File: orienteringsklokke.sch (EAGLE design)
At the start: 15 parts

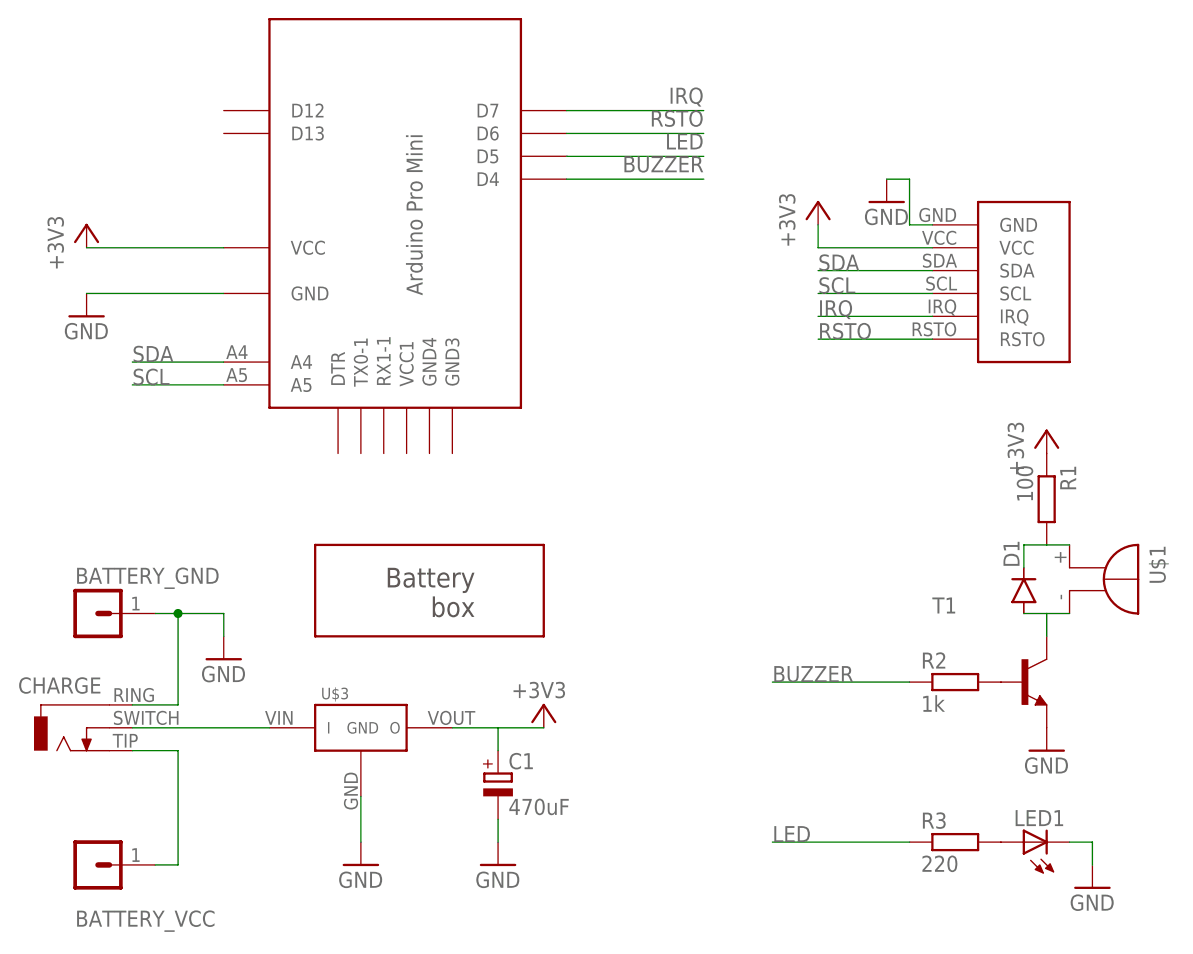
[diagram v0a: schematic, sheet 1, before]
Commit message: Fully traced with jack, switch, buzzer and no battery box
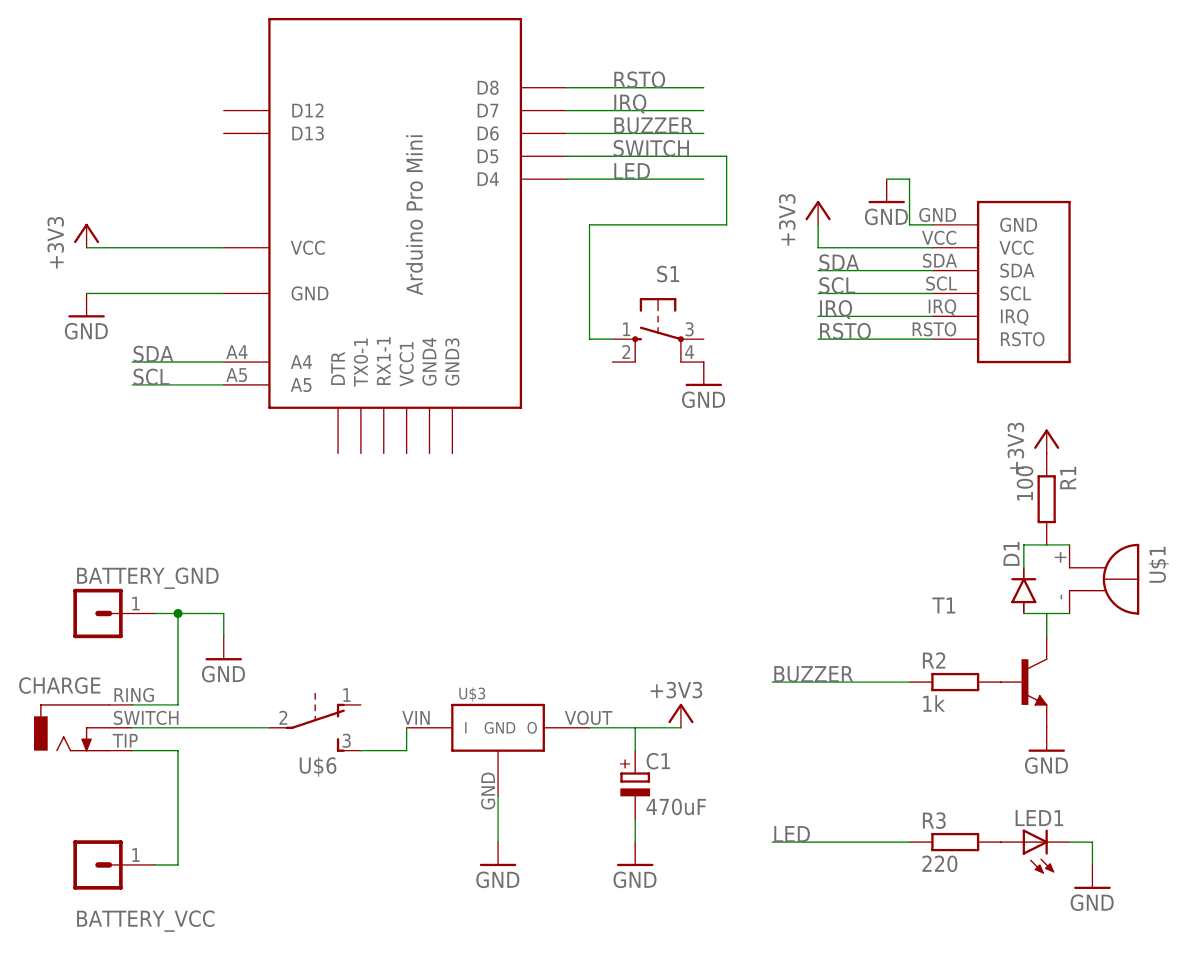
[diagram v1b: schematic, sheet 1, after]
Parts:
- removed U$5: BATTERY-BOX, joakim:BATTERY-BOX
- added S1: (no value), switch-omron:10-XX
- added U$6: SK12D07-SLIDE-SWITCH, joakim:SK12D07-SLIDE-SWITCH
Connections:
- new net N$1: CHARGE.2, U$6.2
- new net SWITCH: S1.S, U$4.D5
- net BUZZER: now also U$4.D6; no longer U$4.D4
- net GND: now also S1.P1
- net LED: now also U$4.D4; no longer U$4.D5
- net N$7: now also U$6.3; no longer CHARGE.2
- net RSTO: now also U$4.D8; no longer U$4.D6
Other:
- moved on the sheet: C1, U$3
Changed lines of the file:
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@@
 <part name="GND7" library="supply1" deviceset="GND" device=""/>
 <part name="CHARGE" library="joakim" deviceset="ST613-JACK" device=""/>
-<part name="U$5" library="joakim" deviceset="BATTERY-BOX" device=""/>
+<part name="S1" library="switch-omron" deviceset="10-XX" device=""/>
+<part name="GND8" library="supply1" deviceset="GND" device=""/>
+<part name="U$6" library="joakim" deviceset="SK12D07-SLIDE-SWITCH" device=""/>
 </parts>
 <sheets>
@@
 </instance>
 <instance part="R3" gate="G$1" x="60.96" y="25.4"/>
-<instance part="C1" gate="G$1" x="10.16" y="33.02"/>
+<instance part="C1" gate="G$1" x="25.4" y="33.02"/>
 <instance part="GND1" gate="1" x="71.12" y="35.56"/>
 <instance part="D1" gate="G$1" x="68.58" y="53.34" smashed="yes" rot="R90">
@@
 <instance part="LED1" gate="G$1" x="68.58" y="25.4" rot="R90"/>
 <instance part="GND2" gate="1" x="76.2" y="20.32"/>
-<instance part="U$3" gate="G$1" x="-5.08" y="38.1"/>
-<instance part="GND3" gate="1" x="-5.08" y="22.86"/>
-<instance part="GND4" gate="1" x="10.16" y="22.86"/>
-<instance part="+3V2" gate="G$1" x="15.24" y="40.64" smashed="yes">
-<attribute name="VALUE" x="17.78" y="43.18" size="1.778" layer="96" rot="R180"/>
+<instance part="U$3" gate="G$1" x="10.16" y="38.1"/>
+<instance part="GND3" gate="1" x="10.16" y="22.86"/>
+<instance part="GND4" gate="1" x="25.4" y="22.86"/>
+<instance part="+3V2" gate="G$1" x="30.48" y="40.64" smashed="yes">
+<attribute name="VALUE" x="33.02" y="43.18" size="1.778" layer="96" rot="R180"/>
 </instance>
 <instance part="GND5" gate="1" x="-20.32" y="45.72"/>
@@
 <attribute name="NAME" x="-43.18" y="41.91" size="1.778" layer="95"/>
 </instance>
-<instance part="U$5" gate="G$1" x="2.54" y="53.34" rot="R180"/>
+<instance part="S1" gate="1" x="27.94" y="81.28" rot="MR270"/>
+<instance part="GND8" gate="1" x="33.02" y="76.2"/>
+<instance part="U$6" gate="G$1" x="-10.16" y="38.1"/>
 </instances>
 <busses>
@@
 <pinref part="U$3" gate="G$1" pin="GND"/>
 <pinref part="GND3" gate="1" pin="GND"/>
-<wire x1="-5.08" y1="25.4" x2="-5.08" y2="30.48" width="0.1524" layer="91"/>
+<wire x1="10.16" y1="25.4" x2="10.16" y2="30.48" width="0.1524" layer="91"/>
 </segment>
 <segment>
 <pinref part="C1" gate="G$1" pin="-"/>
 <pinref part="GND4" gate="1" pin="GND"/>
-<wire x1="10.16" y1="27.94" x2="10.16" y2="25.4" width="0.1524" layer="91"/>
+<wire x1="25.4" y1="27.94" x2="25.4" y2="25.4" width="0.1524" layer="91"/>
 </segment>
 <segment>
@@
 <pinref part="GND7" gate="1" pin="GND"/>
 </segment>
+<segment>
+<pinref part="S1" gate="1" pin="P1"/>
+<pinref part="GND8" gate="1" pin="GND"/>
+</segment>
 </net>
 <net name="N$2" class="0">
@@
 <pinref part="U$3" gate="G$1" pin="VOUT"/>
 <pinref part="C1" gate="G$1" pin="+"/>
-<wire x1="5.08" y1="38.1" x2="10.16" y2="38.1" width="0.1524" layer="91"/>
-<wire x1="10.16" y1="35.56" x2="10.16" y2="38.1" width="0.1524" layer="91"/>
-<wire x1="10.16" y1="38.1" x2="15.24" y2="38.1" width="0.1524" layer="91"/>
+<wire x1="20.32" y1="38.1" x2="25.4" y2="38.1" width="0.1524" layer="91"/>
+<wire x1="25.4" y1="35.56" x2="25.4" y2="38.1" width="0.1524" layer="91"/>
+<wire x1="25.4" y1="38.1" x2="30.48" y2="38.1" width="0.1524" layer="91"/>
 <pinref part="+3V2" gate="G$1" pin="+3V3"/>
 </segment>
@@
 </segment>
 <segment>
-<pinref part="U$4" gate="G$1" pin="D4"/>
-<wire x1="17.78" y1="99.06" x2="33.02" y2="99.06" width="0.1524" layer="91"/>
-<label x="33.02" y="101.6" size="1.778" layer="95" rot="R180"/>
+<pinref part="U$4" gate="G$1" pin="D6"/>
+<wire x1="17.78" y1="104.14" x2="33.02" y2="104.14" width="0.1524" layer="91"/>
+<label x="22.86" y="104.14" size="1.778" layer="95"/>
 </segment>
 </net>
@@
 </segment>
 <segment>
-<pinref part="U$4" gate="G$1" pin="D5"/>
-<wire x1="17.78" y1="101.6" x2="33.02" y2="101.6" width="0.1524" layer="91"/>
-<label x="33.02" y="104.14" size="1.778" layer="95" rot="R180"/>
+<pinref part="U$4" gate="G$1" pin="D4"/>
+<wire x1="17.78" y1="99.06" x2="33.02" y2="99.06" width="0.1524" layer="91"/>
+<label x="22.86" y="99.06" size="1.778" layer="95"/>
 </segment>
 </net>
@@
 <pinref part="U$4" gate="G$1" pin="D7"/>
 <wire x1="17.78" y1="106.68" x2="33.02" y2="106.68" width="0.1524" layer="91"/>
-<label x="33.02" y="109.22" size="1.778" layer="95" rot="R180"/>
+<label x="22.86" y="106.68" size="1.778" layer="95"/>
 </segment>
 </net>
@@
 </segment>
 <segment>
-<pinref part="U$4" gate="G$1" pin="D6"/>
-<wire x1="17.78" y1="104.14" x2="33.02" y2="104.14" width="0.1524" layer="91"/>
-<label x="33.02" y="106.68" size="1.778" layer="95" rot="R180"/>
+<pinref part="U$4" gate="G$1" pin="D8"/>
+<wire x1="17.78" y1="109.22" x2="33.02" y2="109.22" width="0.1524" layer="91"/>
+<label x="22.86" y="109.22" size="1.778" layer="95"/>
 </segment>
 </net>
@@
 </segment>
 </net>
+<net name="SWITCH" class="0">
+<segment>
+<pinref part="U$4" gate="G$1" pin="D5"/>
+<wire x1="17.78" y1="101.6" x2="35.56" y2="101.6" width="0.1524" layer="91"/>
+<label x="22.86" y="101.6" size="1.778" layer="95"/>
+<pinref part="S1" gate="1" pin="S"/>
+<wire x1="22.86" y1="81.28" x2="20.32" y2="81.28" width="0.1524" layer="91"/>
+<wire x1="20.32" y1="81.28" x2="20.32" y2="93.98" width="0.1524" layer="91"/>
+<wire x1="20.32" y1="93.98" x2="35.56" y2="93.98" width="0.1524" layer="91"/>
+<wire x1="35.56" y1="93.98" x2="35.56" y2="101.6" width="0.1524" layer="91"/>
+</segment>
+</net>
+<net name="N$1" class="0">
+<segment>
+<pinref part="CHARGE" gate="G$1" pin="2"/>
+<pinref part="U$6" gate="G$1" pin="2"/>
+<wire x1="-30.48" y1="38.1" x2="-15.24" y2="38.1" width="0.1524" layer="91"/>
+</segment>
+</net>
 <net name="N$7" class="0">
 <segment>
-<pinref part="CHARGE" gate="G$1" pin="2"/>
-<wire x1="-30.48" y1="38.1" x2="-15.24" y2="38.1" width="0.1524" layer="91"/>
+<pinref part="U$6" gate="G$1" pin="3"/>
 <pinref part="U$3" gate="G$1" pin="VIN"/>
+<wire x1="-5.08" y1="35.56" x2="0" y2="35.56" width="0.1524" layer="91"/>
+<wire x1="0" y1="35.56" x2="0" y2="38.1" width="0.1524" layer="91"/>
 </segment>
 </net>
@@
 </schematic>
 </drawing>
-<compatibility>
-<note version="6.3" minversion="6.2.2" severity="warning">
-Since Version 6.2.2 text objects can contain more than one line,
-which will not be processed correctly with this version.
-</note>
-</compatibility>
 </eagle>
